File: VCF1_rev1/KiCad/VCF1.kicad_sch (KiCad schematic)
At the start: 22 parts, among them U14 74HC4053, U15 CEM3350, U16 Opamp_Quad

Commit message: Lot of work on panel etc.
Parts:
- renumbered C16 to C15, C17 to C16, C18 to C17, R74 to R84, R75 to R85, R76 to R86, R77 to R87, R78 to R88, R79 to R89, R80 to R90, R81 to R91, R82 to R92, R83 to R93, R84 to R94, R85 to R95, U14 to U15, U15 to U16, U16 to U17

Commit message: Cleaned up the first page with the overview and tried to make it a bit more readable.
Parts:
- renumbered R90 to R100, R91 to R101, R92 to R102, R93 to R103, R94 to R104, R95 to R105, R84 to R94, R85 to R95, R86 to R96, R87 to R97, R88 to R98, R89 to R99
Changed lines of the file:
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@@
 (kicad_sch (version 20210621) (generator eeschema)
   (paper "A4")
+  (junction (at 135.89 105.41) (diameter 0) (color 0 0 0 0))
+  (junction (at 72.39 106.68) (diameter 0) (color 0 0 0 0))
   (junction (at 152.4 105.41) (diameter 0) (color 0 0 0 0))
+  (junction (at 135.89 69.85) (diameter 0) (color 0 0 0 0))
+  (junction (at 82.55 88.9) (diameter 0) (color 0 0 0 0))
+  (junction (at 96.52 106.68) (diameter 0) (color 0 0 0 0))
+  (junction (at 62.23 96.52) (diameter 0) (color 0 0 0 0))
+  (junction (at 152.4 69.85) (diameter 0) (color 0 0 0 0))
+  (junction (at 114.3 93.98) (diameter 0) (color 0 0 0 0))
+  (junction (at 152.4 144.78) (diameter 0) (color 0 0 0 0))
+  (junction (at 152.4 96.52) (diameter 0) (color 0 0 0 0))
+  (junction (at 72.39 93.98) (diameter 0) (color 0 0 0 0))
+  (junction (at 152.4 134.62) (diameter 0) (color 0 0 0 0))
+  (junction (at 127 134.62) (diameter 0) (color 0 0 0 0))
+  (junction (at 92.71 88.9) (diameter 0) (color 0 0 0 0))
+  (junction (at 152.4 124.46) (diameter 0) (color 0 0 0 0))
   (junction (at 127 91.44) (diameter 0) (color 0 0 0 0))
-  (junction (at 135.89 105.41) (diameter 0) (color 0 0 0 0))
-  (junction (at 96.52 106.68) (diameter 0) (color 0 0 0 0))
   (junction (at 82.55 106.68) (diameter 0) (color 0 0 0 0))
-  (junction (at 72.39 106.68) (diameter 0) (color 0 0 0 0))
-  (junction (at 152.4 124.46) (diameter 0) (color 0 0 0 0))
-  (junction (at 152.4 144.78) (diameter 0) (color 0 0 0 0))
-  (junction (at 72.39 93.98) (diameter 0) (color 0 0 0 0))
-  (junction (at 114.3 93.98) (diameter 0) (color 0 0 0 0))
-  (junction (at 62.23 96.52) (diameter 0) (color 0 0 0 0))
-  (junction (at 127 134.62) (diameter 0) (color 0 0 0 0))
-  (junction (at 135.89 69.85) (diameter 0) (color 0 0 0 0))
-  (junction (at 152.4 134.62) (diameter 0) (color 0 0 0 0))
-  (junction (at 92.71 88.9) (diameter 0) (color 0 0 0 0))
-  (junction (at 152.4 96.52) (diameter 0) (color 0 0 0 0))
-  (junction (at 152.4 69.85) (diameter 0) (color 0 0 0 0))
-  (junction (at 82.55 88.9) (diameter 0) (color 0 0 0 0))
   (junction (at 127 144.78) (diameter 0) (color 0 0 0 0))
   (wire (pts (xy 127 144.78) (xy 127 146.05))
@@
     (stroke (width 0) (type default) (color 0 0 0 0))
   )
+  (wire (pts (xy 82.55 88.9) (xy 92.71 88.9))
+    (stroke (width 0) (type default) (color 0 0 0 0))
+  )
   (wire (pts (xy 92.71 88.9) (xy 97.79 88.9))
-    (stroke (width 0) (type default) (color 0 0 0 0))
-  )
-  (wire (pts (xy 82.55 88.9) (xy 92.71 88.9))
     (stroke (width 0) (type default) (color 0 0 0 0))
   )
@@
   (symbol (lib_id "Device:R") (at 82.55 101.6 0)
     (in_bom yes) (on_board yes) (fields_autoplaced)
-    (property "Reference" "R87" (id 0) (at 85.09 100.3299 0)
+    (property "Reference" "R97" (id 0) (at 85.09 100.3299 0)
       (effects (font (size 1.27 1.27)) (justify left))
     )
@@
   (symbol (lib_id "power:GND") (at 127 154.94 0)
     (in_bom yes) (on_board yes) (fields_autoplaced)
-    (property "Reference" "#PWR037" (id 0) (at 127 161.29 0)
+    (property "Reference" "#PWR047" (id 0) (at 127 161.29 0)
       (effects (font (size 1.27 1.27)) hide)
     )
@@
   (symbol (lib_id "Device:R") (at 82.55 83.82 0)
     (in_bom yes) (on_board yes) (fields_autoplaced)
-    (property "Reference" "R86" (id 0) (at 85.09 82.5499 0)
+    (property "Reference" "R96" (id 0) (at 85.09 82.5499 0)
       (effects (font (size 1.27 1.27)) (justify left))
     )
@@
   (symbol (lib_id "Device:R") (at 152.4 149.86 0)
     (in_bom yes) (on_board yes) (fields_autoplaced)
-    (property "Reference" "R95" (id 0) (at 154.94 148.5899 0)
+    (property "Reference" "R105" (id 0) (at 154.94 148.5899 0)
       (effects (font (size 1.27 1.27)) (justify left))
     )
@@
   (symbol (lib_id "Device:R") (at 72.39 101.6 0)
     (in_bom yes) (on_board yes)
-    (property "Reference" "R85" (id 0) (at 74.93 100.3299 0)
+    (property "Reference" "R95" (id 0) (at 74.93 100.3299 0)
       (effects (font (size 1.27 1.27)) (justify left))
     )
@@
   (symbol (lib_id "Device:R") (at 147.32 69.85 90)
     (in_bom yes) (on_board yes) (fields_autoplaced)
-    (property "Reference" "R92" (id 0) (at 147.32 63.5 90))
+    (property "Reference" "R102" (id 0) (at 147.32 63.5 90))
     (property "Value" "22kΩ" (id 1) (at 147.32 66.04 90))
     (property "Footprint" "" (id 2) (at 147.32 71.628 90)
@@
   (symbol (lib_id "Device:R") (at 135.89 110.49 0)
     (in_bom yes) (on_board yes) (fields_autoplaced)
-    (property "Reference" "R91" (id 0) (at 138.43 109.2199 0)
+    (property "Reference" "R101" (id 0) (at 138.43 109.2199 0)
       (effects (font (size 1.27 1.27)) (justify left))
     )
@@
   (symbol (lib_id "power:GND") (at 135.89 80.01 0)
     (in_bom yes) (on_board yes) (fields_autoplaced)
-    (property "Reference" "#PWR038" (id 0) (at 135.89 86.36 0)
+    (property "Reference" "#PWR048" (id 0) (at 135.89 86.36 0)
       (effects (font (size 1.27 1.27)) hide)
     )
@@
   (symbol (lib_id "Device:R") (at 127 149.86 0)
     (in_bom yes) (on_board yes) (fields_autoplaced)
-    (property "Reference" "R89" (id 0) (at 129.54 148.5899 0)
+    (property "Reference" "R99" (id 0) (at 129.54 148.5899 0)
       (effects (font (size 1.27 1.27)) (justify left))
     )
@@
   (symbol (lib_id "Device:R") (at 152.4 129.54 180)
     (in_bom yes) (on_board yes) (fields_autoplaced)
-    (property "Reference" "R94" (id 0) (at 154.94 128.2699 0)
+    (property "Reference" "R104" (id 0) (at 154.94 128.2699 0)
       (effects (font (size 1.27 1.27)) (justify right))
     )
@@
   (symbol (lib_id "Device:R") (at 97.79 124.46 90)
     (in_bom yes) (on_board yes) (fields_autoplaced)
-    (property "Reference" "R88" (id 0) (at 97.79 118.11 90))
+    (property "Reference" "R98" (id 0) (at 97.79 118.11 90))
     (property "Value" "330kΩ" (id 1) (at 97.79 120.65 90))
     (property "Footprint" "" (id 2) (at 97.79 126.238 90)
@@
   (symbol (lib_id "Device:R") (at 135.89 74.93 0)
     (in_bom yes) (on_board yes) (fields_autoplaced)
-    (property "Reference" "R90" (id 0) (at 138.43 73.6599 0)
+    (property "Reference" "R100" (id 0) (at 138.43 73.6599 0)
       (effects (font (size 1.27 1.27)) (justify left))
     )
@@
   (symbol (lib_id "Device:R") (at 147.32 105.41 90)
     (in_bom yes) (on_board yes) (fields_autoplaced)
-    (property "Reference" "R93" (id 0) (at 147.32 99.06 90))
+    (property "Reference" "R103" (id 0) (at 147.32 99.06 90))
     (property "Value" "22kΩ" (id 1) (at 147.32 101.6 90))
     (property "Footprint" "" (id 2) (at 147.32 107.188 90)
@@
   (symbol (lib_id "Device:R") (at 62.23 101.6 0)
     (in_bom yes) (on_board yes)
-    (property "Reference" "R84" (id 0) (at 64.77 100.3299 0)
+    (property "Reference" "R94" (id 0) (at 64.77 100.3299 0)
       (effects (font (size 1.27 1.27)) (justify left))
     )
@@
   (symbol (lib_id "power:GND") (at 96.52 107.95 0)
     (in_bom yes) (on_board yes) (fields_autoplaced)
-    (property "Reference" "#PWR036" (id 0) (at 96.52 114.3 0)
+    (property "Reference" "#PWR046" (id 0) (at 96.52 114.3 0)
       (effects (font (size 1.27 1.27)) hide)
     )
@@
   (symbol (lib_id "power:GND") (at 135.89 115.57 0)
     (in_bom yes) (on_board yes) (fields_autoplaced)
-    (property "Reference" "#PWR039" (id 0) (at 135.89 121.92 0)
+    (property "Reference" "#PWR049" (id 0) (at 135.89 121.92 0)
       (effects (font (size 1.27 1.27)) hide)
     )
@@
   (symbol (lib_id "power:GND") (at 152.4 154.94 0)
     (in_bom yes) (on_board yes) (fields_autoplaced)
-    (property "Reference" "#PWR040" (id 0) (at 152.4 161.29 0)
-      (effects (font (size 1.27 1.27)) hide)
-    )
+    (property "Reference" "#PWR050" (id 0) (at 152.4 161.29 0)
+      (effects (font (size 1.27 1.27)) hide)
+    )

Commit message: Drew a better symbol for LM13700 because the other one was ugly.
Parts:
- R100, R101, R102, R103, R104, R105, R94, R95, R96, R97, R98, R99: footprint (none) -> Resistor_SMD:R_0603_1608Metric
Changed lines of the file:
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@@
 (kicad_sch (version 20210621) (generator eeschema)
   (paper "A4")
-  (junction (at 135.89 105.41) (diameter 0) (color 0 0 0 0))
-  (junction (at 72.39 106.68) (diameter 0) (color 0 0 0 0))
-  (junction (at 152.4 105.41) (diameter 0) (color 0 0 0 0))
-  (junction (at 135.89 69.85) (diameter 0) (color 0 0 0 0))
-  (junction (at 82.55 88.9) (diameter 0) (color 0 0 0 0))
-  (junction (at 96.52 106.68) (diameter 0) (color 0 0 0 0))
+  (junction (at 127 144.78) (diameter 0) (color 0 0 0 0))
+  (junction (at 127 91.44) (diameter 0) (color 0 0 0 0))
+  (junction (at 127 134.62) (diameter 0) (color 0 0 0 0))
+  (junction (at 152.4 96.52) (diameter 0) (color 0 0 0 0))
   (junction (at 62.23 96.52) (diameter 0) (color 0 0 0 0))
   (junction (at 152.4 69.85) (diameter 0) (color 0 0 0 0))
+  (junction (at 135.89 69.85) (diameter 0) (color 0 0 0 0))
+  (junction (at 82.55 106.68) (diameter 0) (color 0 0 0 0))
+  (junction (at 82.55 88.9) (diameter 0) (color 0 0 0 0))
+  (junction (at 152.4 105.41) (diameter 0) (color 0 0 0 0))
   (junction (at 114.3 93.98) (diameter 0) (color 0 0 0 0))
+  (junction (at 152.4 134.62) (diameter 0) (color 0 0 0 0))
   (junction (at 152.4 144.78) (diameter 0) (color 0 0 0 0))
-  (junction (at 152.4 96.52) (diameter 0) (color 0 0 0 0))
+  (junction (at 92.71 88.9) (diameter 0) (color 0 0 0 0))
+  (junction (at 96.52 106.68) (diameter 0) (color 0 0 0 0))
+  (junction (at 152.4 124.46) (diameter 0) (color 0 0 0 0))
+  (junction (at 72.39 106.68) (diameter 0) (color 0 0 0 0))
   (junction (at 72.39 93.98) (diameter 0) (color 0 0 0 0))
-  (junction (at 152.4 134.62) (diameter 0) (color 0 0 0 0))
-  (junction (at 127 134.62) (diameter 0) (color 0 0 0 0))
-  (junction (at 92.71 88.9) (diameter 0) (color 0 0 0 0))
-  (junction (at 152.4 124.46) (diameter 0) (color 0 0 0 0))
-  (junction (at 127 91.44) (diameter 0) (color 0 0 0 0))
-  (junction (at 82.55 106.68) (diameter 0) (color 0 0 0 0))
-  (junction (at 127 144.78) (diameter 0) (color 0 0 0 0))
+  (junction (at 135.89 105.41) (diameter 0) (color 0 0 0 0))
   (wire (pts (xy 127 144.78) (xy 127 146.05))
     (stroke (width 0) (type default) (color 0 0 0 0))
@@
       (effects (font (size 1.27 1.27)) (justify left))
     )
-    (property "Footprint" "" (id 2) (at 80.772 101.6 90)
+    (property "Footprint" "Resistor_SMD:R_0603_1608Metric" (id 2) (at 80.772 101.6 90)
       (effects (font (size 1.27 1.27)) hide)
     )
@@
       (effects (font (size 1.27 1.27)) (justify left))
     )
-    (property "Footprint" "" (id 2) (at 80.772 83.82 90)
+    (property "Footprint" "Resistor_SMD:R_0603_1608Metric" (id 2) (at 80.772 83.82 90)
       (effects (font (size 1.27 1.27)) hide)
     )
@@
       (effects (font (size 1.27 1.27)) (justify left))
     )
-    (property "Footprint" "" (id 2) (at 150.622 149.86 90)
+    (property "Footprint" "Resistor_SMD:R_0603_1608Metric" (id 2) (at 150.622 149.86 90)
       (effects (font (size 1.27 1.27)) hide)
     )
@@
       (effects (font (size 1.27 1.27)) (justify left))
     )
-    (property "Footprint" "" (id 2) (at 70.612 101.6 90)
+    (property "Footprint" "Resistor_SMD:R_0603_1608Metric" (id 2) (at 70.612 101.6 90)
       (effects (font (size 1.27 1.27)) hide)
     )
@@
     (property "Reference" "R102" (id 0) (at 147.32 63.5 90))
     (property "Value" "22kΩ" (id 1) (at 147.32 66.04 90))
-    (property "Footprint" "" (id 2) (at 147.32 71.628 90)
+    (property "Footprint" "Resistor_SMD:R_0603_1608Metric" (id 2) (at 147.32 71.628 90)
       (effects (font (size 1.27 1.27)) hide)
     )
@@
       (effects (font (size 1.27 1.27)) (justify left))
     )
-    (property "Footprint" "" (id 2) (at 134.112 110.49 90)
+    (property "Footprint" "Resistor_SMD:R_0603_1608Metric" (id 2) (at 134.112 110.49 90)
       (effects (font (size 1.27 1.27)) hide)
     )
@@
       (effects (font (size 1.27 1.27)) (justify left))
     )
-    (property "Footprint" "" (id 2) (at 125.222 149.86 90)
+    (property "Footprint" "Resistor_SMD:R_0603_1608Metric" (id 2) (at 125.222 149.86 90)
       (effects (font (size 1.27 1.27)) hide)
     )
@@
       (effects (font (size 1.27 1.27)) (justify right))
     )
-    (property "Footprint" "" (id 2) (at 154.178 129.54 90)
+    (property "Footprint" "Resistor_SMD:R_0603_1608Metric" (id 2) (at 154.178 129.54 90)
       (effects (font (size 1.27 1.27)) hide)
     )
@@
     (property "Reference" "R98" (id 0) (at 97.79 118.11 90))
     (property "Value" "330kΩ" (id 1) (at 97.79 120.65 90))
-    (property "Footprint" "" (id 2) (at 97.79 126.238 90)
+    (property "Footprint" "Resistor_SMD:R_0603_1608Metric" (id 2) (at 97.79 126.238 90)
       (effects (font (size 1.27 1.27)) hide)
     )
@@
       (effects (font (size 1.27 1.27)) (justify left))
     )
-    (property "Footprint" "" (id 2) (at 134.112 74.93 90)
+    (property "Footprint" "Resistor_SMD:R_0603_1608Metric" (id 2) (at 134.112 74.93 90)
       (effects (font (size 1.27 1.27)) hide)
     )
@@
     (property "Reference" "R103" (id 0) (at 147.32 99.06 90))
     (property "Value" "22kΩ" (id 1) (at 147.32 101.6 90))
-    (property "Footprint" "" (id 2) (at 147.32 107.188 90)
+    (property "Footprint" "Resistor_SMD:R_0603_1608Metric" (id 2) (at 147.32 107.188 90)
       (effects (font (size 1.27 1.27)) hide)
     )
@@
       (effects (font (size 1.27 1.27)) (justify left))
     )
-    (property "Footprint" "" (id 2) (at 60.452 101.6 90)
-      (effects (font (size 1.27 1.27)) hide)
-    )
+    (property "Footprint" "Resistor_SMD:R_0603_1608Metric" (id 2) (at 60.452 101.6 90)
+      (effects (font (size 1.27 1.27)) hide)
+    )

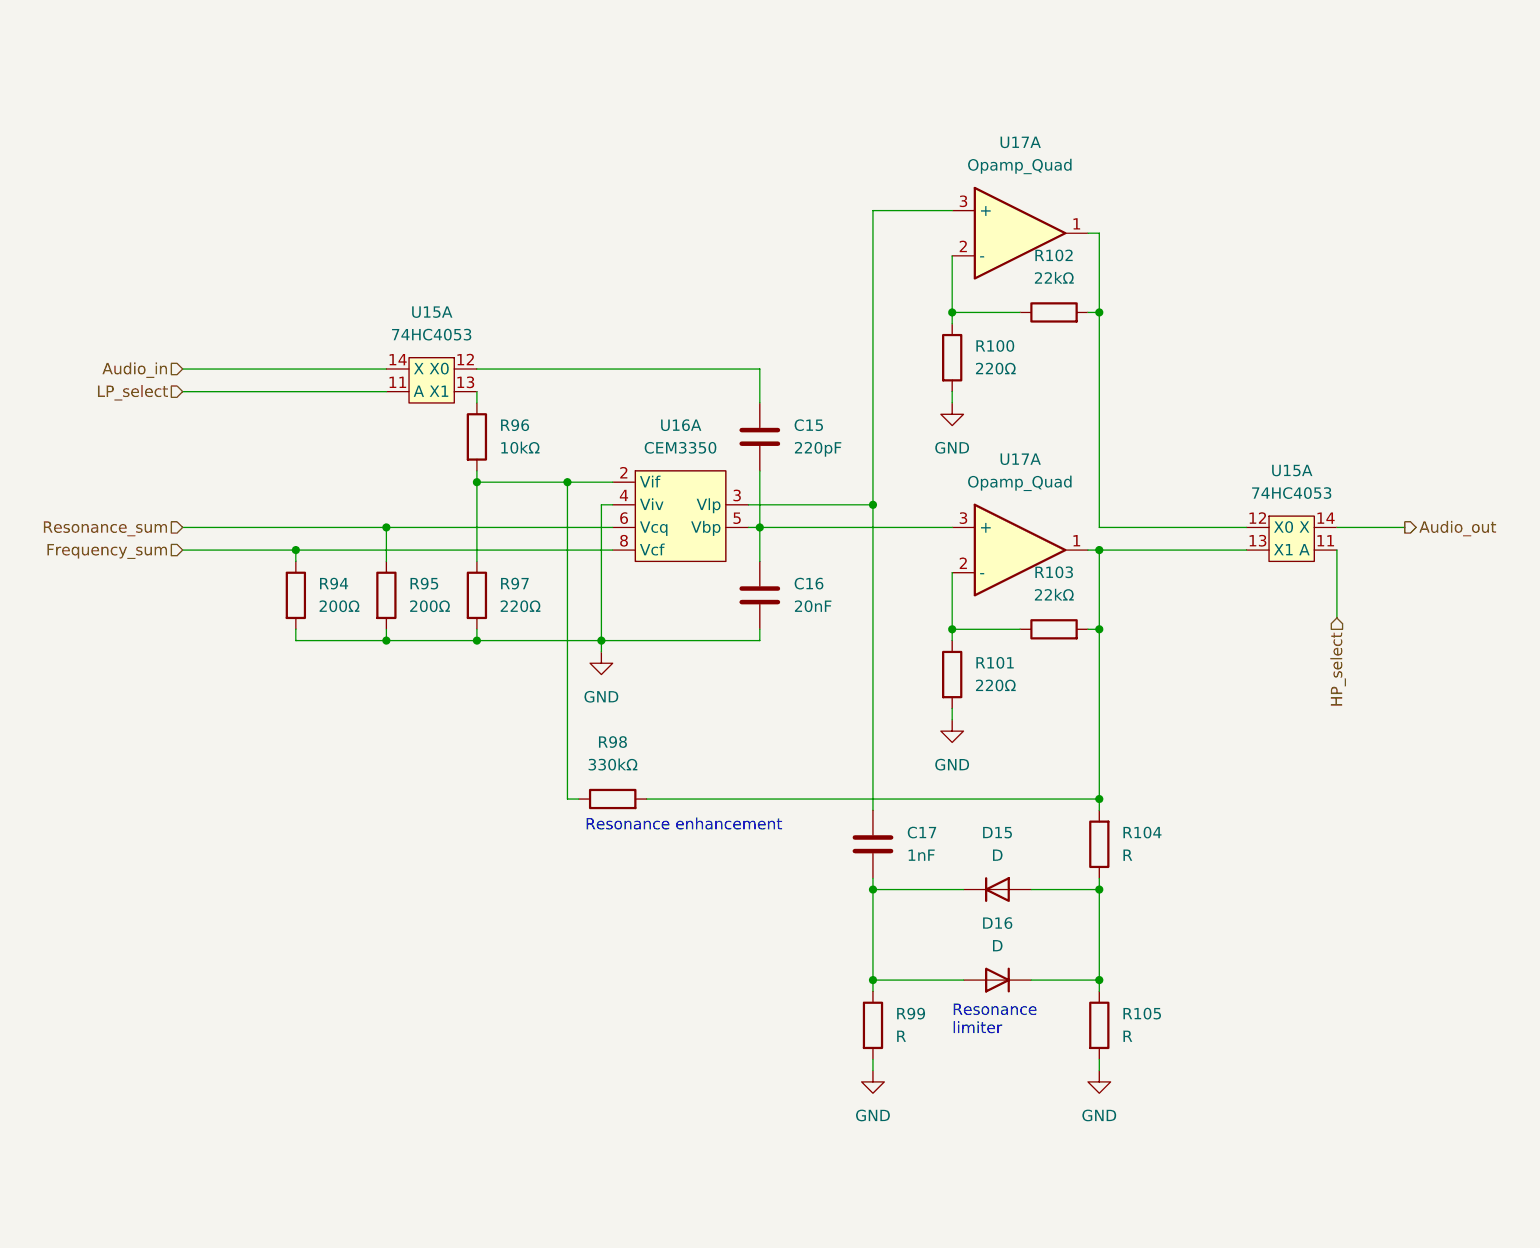
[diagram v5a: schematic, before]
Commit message: Started to populate the PCB and done some small fixes in the schematics.
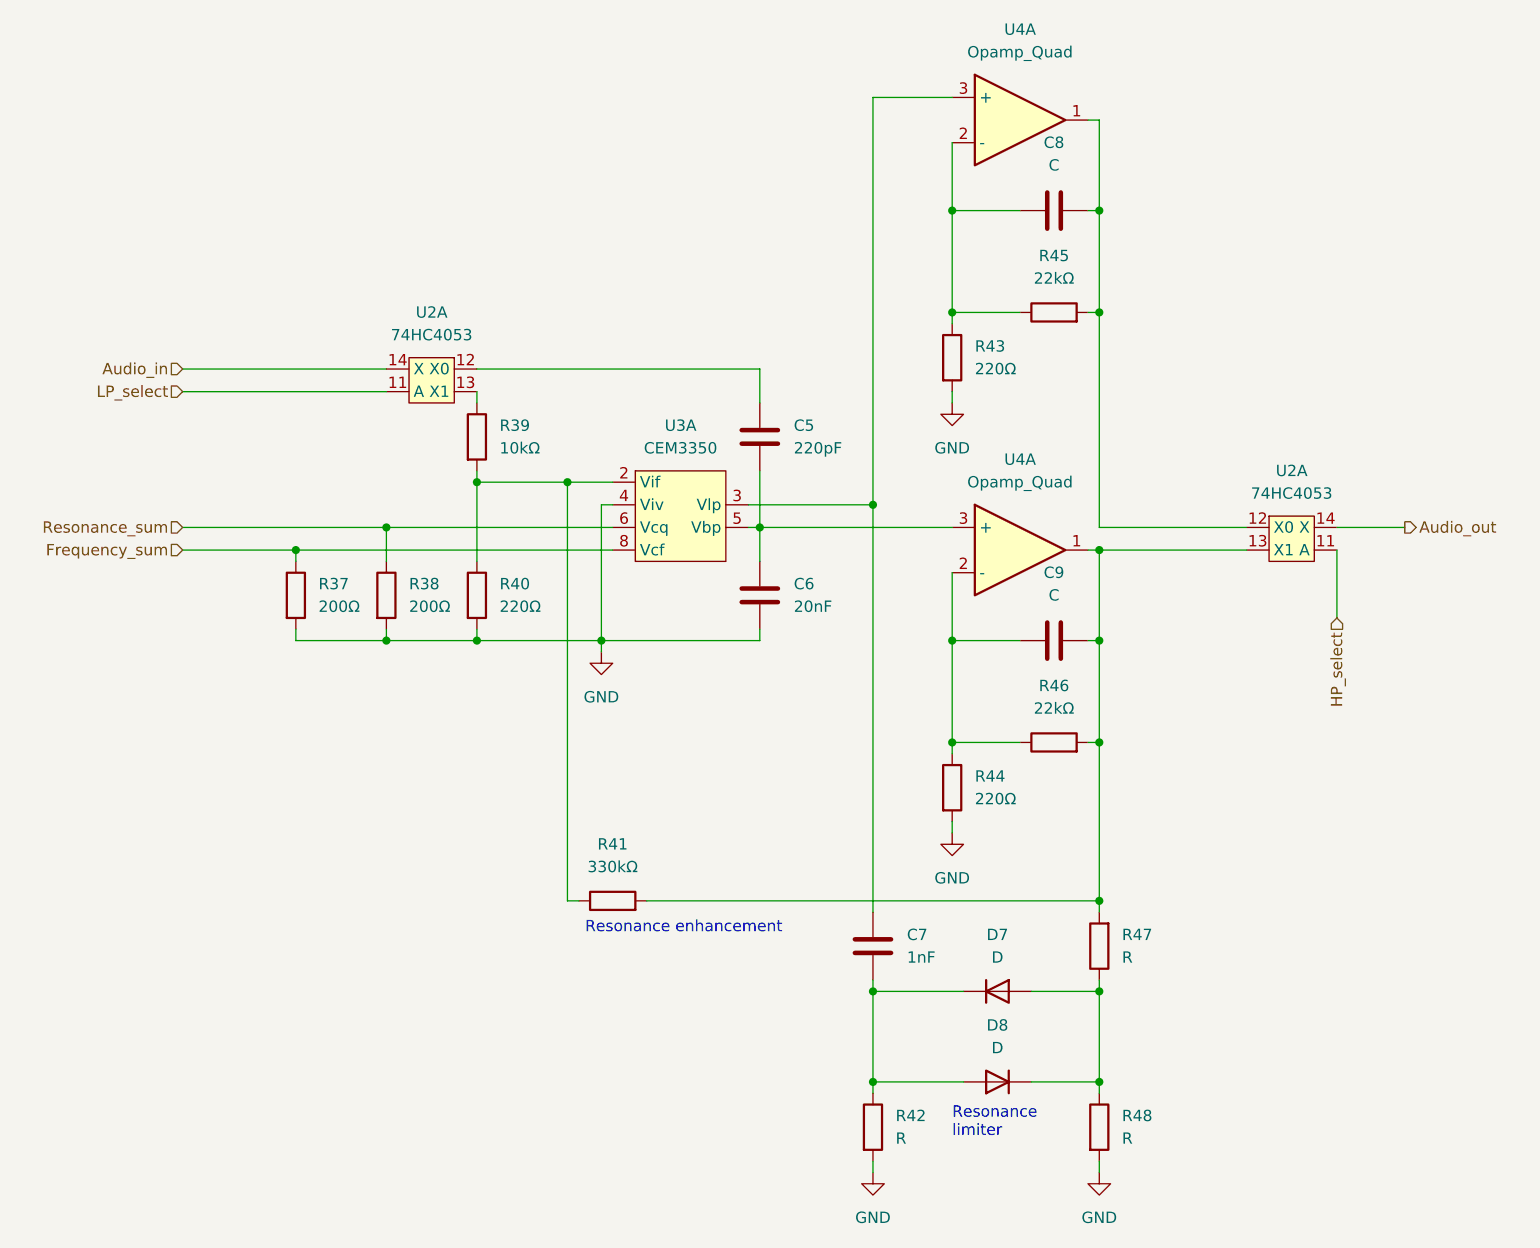
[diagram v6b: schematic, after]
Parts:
- added C8, C9: C, symbol Device:C
- C5: renamed from C15; footprint (none) -> Capacitor_SMD:C_0603_1608Metric
- C6: renamed from C16; footprint (none) -> Capacitor_SMD:C_0603_1608Metric
- C7: renamed from C17; footprint (none) -> Capacitor_SMD:C_0603_1608Metric
- D7: renamed from D15; footprint (none) -> Diode_SMD:D_SOD-123
- D8: renamed from D16; footprint (none) -> Diode_SMD:D_SOD-123
- U2: renamed from U15; footprint (none) -> Package_SO:SOIC-16_3.9x9.9mm_P1.27mm
- U3: renamed from U16; footprint (none) -> Package_SO:SOIC-16_3.9x9.9mm_P1.27mm
- U4: renamed from U17; footprint (none) -> Package_SO:SOIC-14_3.9x8.7mm_P1.27mm
- renumbered R94 to R37, R95 to R38, R96 to R39, R97 to R40, R98 to R41, R99 to R42, R100 to R43, R101 to R44, R102 to R45, R103 to R46, R104 to R47, R105 to R48
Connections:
- net at R45.2, U2.12 (X0), U4.1: now also C8.2
- net at R41.2, R46.2, R47.2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: now also C9.2
- net at R43.1, R45.1, U4.2 (-): now also C8.1
- net at R44.1, R46.1, U4.2 (-): now also C9.1
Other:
- moved on the sheet: C7, D7, D8, R41, R42, R44, R46, R47, R48, U4A
